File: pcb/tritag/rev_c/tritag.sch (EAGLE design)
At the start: 137 parts, among them J1 TC2030-JLINK-NL, J3 MICRO_USB_B_HIROSE_ZX62-B-5PA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, J4 BAT_HOLE, J5 BAT_HOLE, J6 TC2030-JLINK-NL, J7 CON_MICRO_SDDM3AT-SF-PEJM5, T1 HHM1595A1, U1 NRF52840, U12 SIP32510, U2 MCP73831, U3 FT232RQ, U4 MAX8887EZK33+T, U5 STM32F091CC, U6 SKY13317, U7 LXDC2HN18A, U8 DW1000, U9 LIS2DW12, X1 32MHz, X2 38.4M, X3 16M, X4 32.768kHz

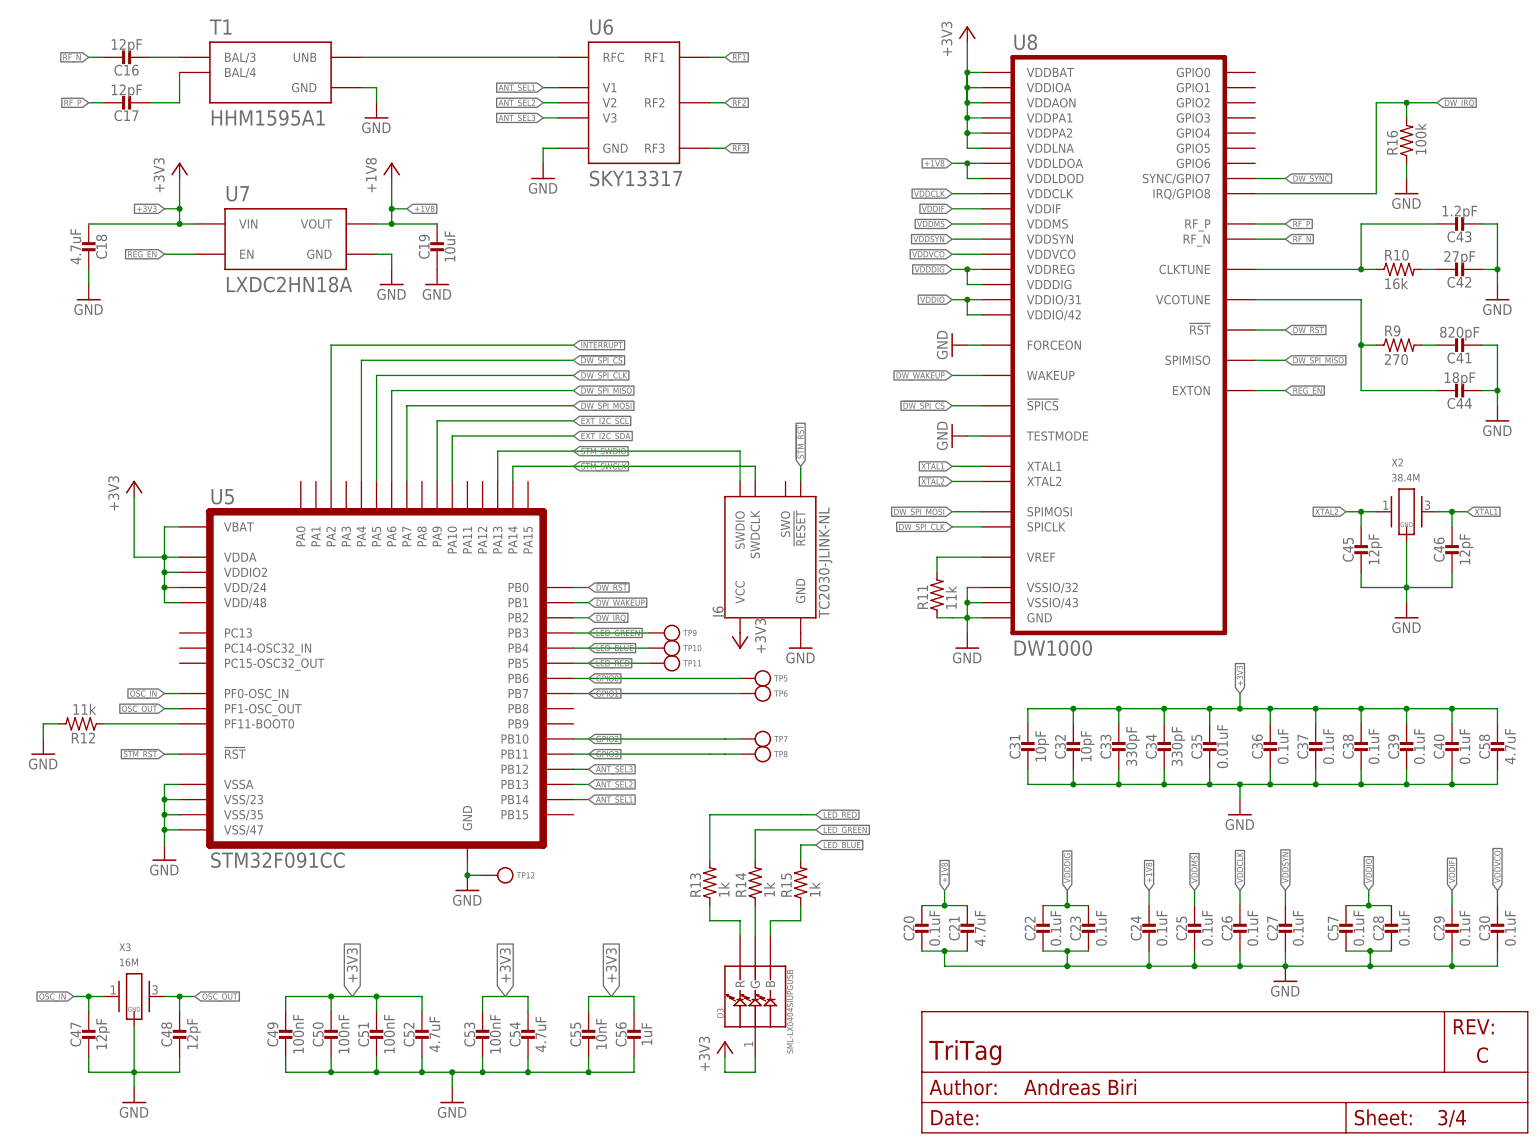
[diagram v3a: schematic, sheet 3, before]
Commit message: carrier board ready for layout
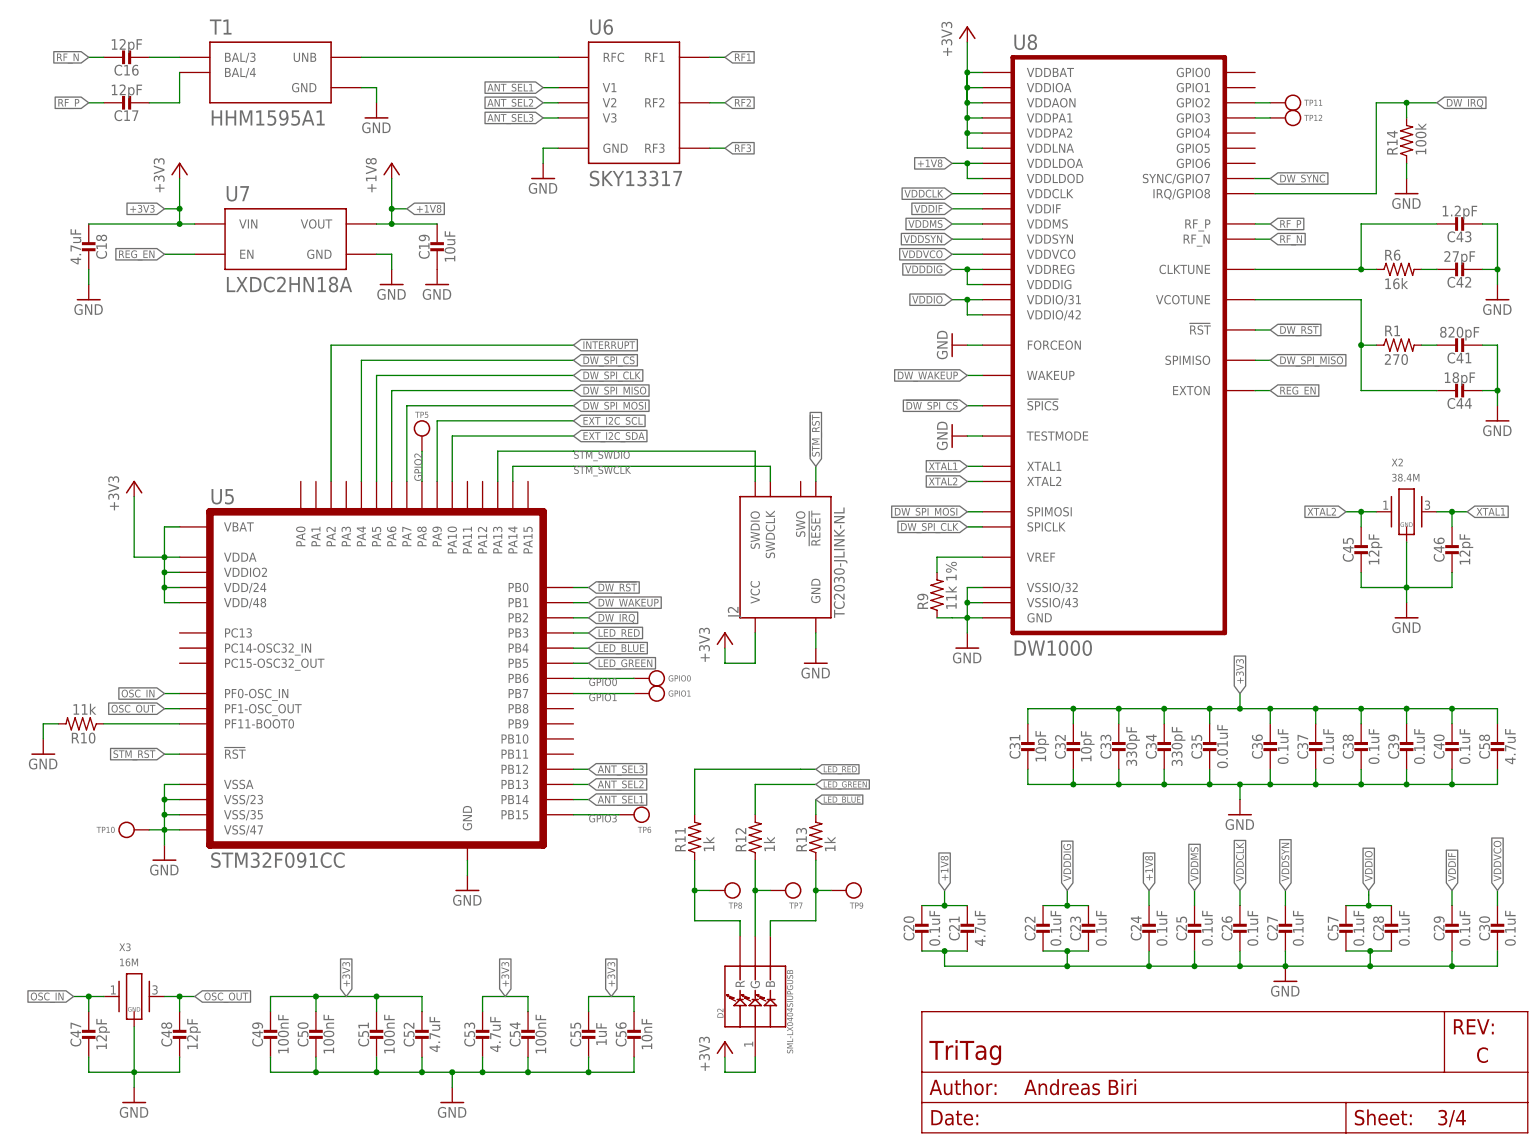
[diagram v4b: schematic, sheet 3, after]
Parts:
- removed J6: TC2030-JLINK-NL, connector:TC2030-JLINK-NL
- removed R15: 1k, passives:RESISTOR0402_RES
- removed R16: 100k, passives:RESISTOR0201_RES
- removed SJ2, SJ3, SJ4, SJ5: SOLDERJUMPERNC2, SparkFun-Passives:SOLDERJUMPERNC2
- added GPIO0, GPIO1: TEST_POINT_0.040IN, headers:TEST_POINT_0.040IN
- added J2: TC2030-JLINK-NL, connector:TC2030-JLINK-NL
- added R1: 270, passives:RESISTOR0402_RES
- added R6: 16k, passives:RESISTOR0402_RES
- added TP13, TP14: TEST-POINT, headers:TEST-POINT
- C18, C21, C58: device passives:CAPACITOR0603_CAP -> passives:CAPACITOR0402_CAP
- C20, C22, C23, C24, C25, C26, C27, C28, C29, C30, C31, C32, C33, C34, C35, C36, C37, C38, C39, C40, C41, C42, C43, C44, C45, C46, C47, C48, C49, C50, C51, C52, C57: device passives:CAPACITOR0201_CAP -> passives:CAPACITOR0402_CAP
- C53: value 100nF -> 4.7uF; device passives:CAPACITOR0201_CAP -> passives:CAPACITOR0402_CAP
- C54: value 4.7uF -> 100nF; device passives:CAPACITOR0201_CAP -> passives:CAPACITOR0402_CAP
- C55: value 10nF -> 1uF; device passives:CAPACITOR0201_CAP -> passives:CAPACITOR0402_CAP
- C56: value 1uF -> 10nF; device passives:CAPACITOR0201_CAP -> passives:CAPACITOR0402_CAP
- R10: value 16k -> 11k; device passives:RESISTOR0201_RES -> passives:RESISTOR0402_RES
- R11, R12: value 11k -> 1k; device passives:RESISTOR0201_RES -> passives:RESISTOR0402_RES
- R14: value 1k -> 100k
- R9: value 270 -> 11k 1%; device passives:RESISTOR0201_RES -> passives:RESISTOR0402_RES
- TP5, TP6: value TEST_POINT_0.040IN -> TEST-POINT; device headers:TEST_POINT_0.040IN -> headers:TEST-POINT
- renumbered D3 to D2
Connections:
- removed net !FTDI_RESET: SJ3.2, U3.!RESET
- removed net FTDI_VCCIO: SJ2.2, U3.VCCIO
- removed net N$28: D2.B, R15.1
- removed net N$29: D2.R, R13.1
- removed net RXD: SJ4.1, U3.RXD
- removed net TXD: SJ5.1, U3.TXD
- removed net VBAT_OK: U1.P1.06
- removed net VCC: C1.1, C11.1, C2.1, C3.1, C5.1, C6.1, C75.1, C76.1, D5.VDD, J1.VCC, R4.2, R5.2, SJ2.1, U1.VDD, U1.VDDH, U12.VSUPP, U4.OUT, U9.VCC, U9.VDD_IO
- new net N$12: C42.1, R6.2
- new net N$14: C44.1, R1.1, U8.VCOTUNE
- new net N$16: C43.1, R6.1, U8.CLKTUNE
- new net N$8: C41.1, R1.2
- new net NRF_GPIO_0: TP13.TESTPOINT, U1.P0.16
- new net NRF_GPIO_1: TP14.TESTPOINT, U1.P0.17
- new net NRF_SWO: J1.SWO, U1.P1.00
- net !RST: now also U3.!RESET; no longer SJ3.1
- net !STM_RST: now also J2.!RESET; no longer J6.!RESET
- net +3V3: now also C1.1, C11.1, C2.1, C3.1, C5.1, C6.1, C75.1, C76.1, D5.VDD, J1.VCC, J2.VCC, R4.2, R5.2, U1.VDD, U1.VDDH, U12.VSUPP, U3.VCCIO, U4.OUT, U9.VCC, U9.VDD_IO; no longer J6.VCC
- net DBG_RX: now also U3.TXD; no longer SJ5.2
- net DBG_TX: now also U3.RXD; no longer SJ4.2
- net DW_IRQ: now also R14.2; no longer R16.2
- net EXT_I2C_SCL: now also U1.P0.13; no longer U1.P0.14, U1.P1.10
- net EXT_I2C_SDA: no longer U1.P1.11
- net GND: now also J2.GND, R10.2, R14.1, R9.1, TP10.TESTPOINT; no longer J6.GND, R11.1, R12.2, R16.1, TP12.TESTPOINT
- net GPIO0: now also GPIO0.TESTPOINT; no longer TP5.TESTPOINT
- net GPIO1: now also GPIO1.TESTPOINT; no longer TP6.TESTPOINT
- net GPIO2: now also TP5.TESTPOINT, U5.PA8; no longer TP7.TESTPOINT, U5.PB10
- net GPIO3: now also TP6.TESTPOINT, U5.PB15; no longer TP8.TESTPOINT, U5.PB11
- net LED_BLUE: now also R13.2; no longer R15.2, TP10.TESTPOINT
- net LED_GREEN: now also R12.2, U5.PB5; no longer R14.2, TP9.TESTPOINT, U5.PB3
- net LED_RED: now also R11.2, U5.PB3; no longer R13.2, TP11.TESTPOINT, U5.PB5
- net N$21: now also U8.VREF; no longer C41.1
- net N$22: now also R10.1, U5.PF11-BOOT0; no longer C42.1, R10.2
- net N$23: now also D2.G, R12.1, TP7.TESTPOINT; no longer C44.1, R9.1, U8.VCOTUNE
- net N$24: now also D2.B, R13.1, TP9.TESTPOINT; no longer C43.1, R10.1, U8.CLKTUNE
- net N$25: now also D2.R, R11.1, TP8.TESTPOINT; no longer R11.2, U8.VREF
- net N$26: now also TP11.TESTPOINT, U8.GPIO2; no longer R12.1, U5.PF11-BOOT0
- net N$27: now also TP12.TESTPOINT, U8.GPIO3; no longer D2.G, R14.1
- net STM_INTERRUPT: now also U1.P0.25; no longer U1.P1.12
- net STM_SWCLK: now also J2.SWDCLK; no longer J6.SWDCLK
- net STM_SWDIO: now also J2.SWDIO; no longer J6.SWDIO
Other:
- note added: "Be aware that the DecaWave is very sensitive regarding its power supply. We suggest using the "MAX8887EZK33+T" from Maxim Integrated. You can find a reference layout at github.com/lab11/polypoint/pcb/tritag."
- note added: "Guarantee 120° offset in-between antennas to maximize polarization difference and antenna diversity RF traces should respect the keepout zones and be surrounded by a via shield. Furthermore, try to keep them as short and straight as possible"
- note added: "Note: Additional I2C pull-up resistors required to +3V3"
- note added: "Power Supply"
- note added: "Signals"
- note added: "VDD/24"
- note added: "VDD/48"
- note removed: "Note: Additional I2C pull-up resistors required"
- note removed: "VDD"
- moved on the sheet: C49, C50, R10, R11, R12, R13, R14, R9, TP10, TP11, TP12, TP5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
